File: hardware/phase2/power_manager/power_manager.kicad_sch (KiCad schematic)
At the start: 80 parts, among them J1 1725656, J2 Conn_02x04_Odd_Even, J3 S2B-PH-K-SLFSN, J4 OSTVN04A150, J5 10118194-0001LF, U1 LTC3586EUFE-PBF, U2 TPS60403DBVR, U3 TPS73225DBVR, U4 TPS72325DBVR

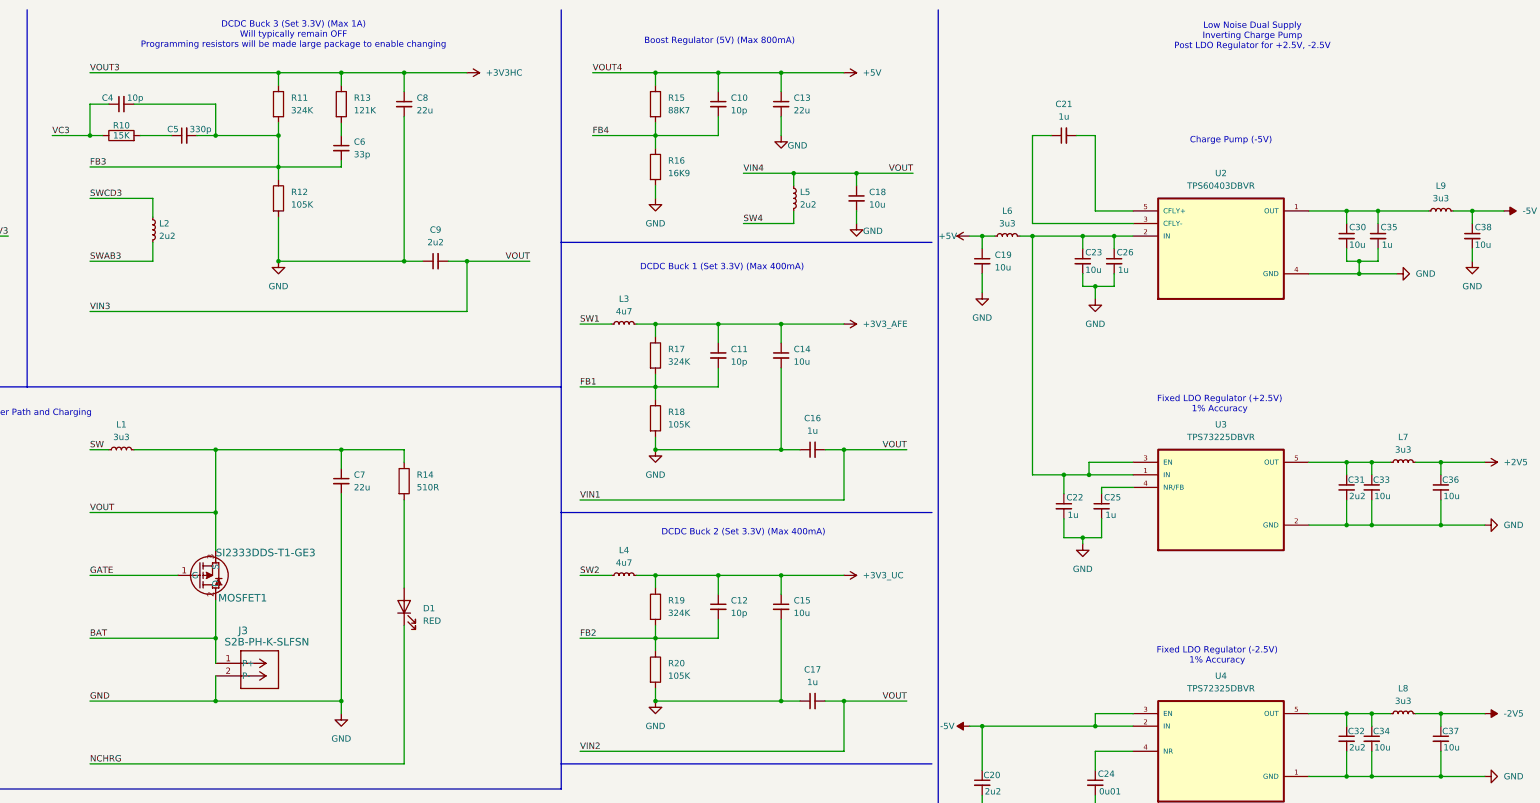
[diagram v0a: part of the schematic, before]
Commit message: Update text on schematic
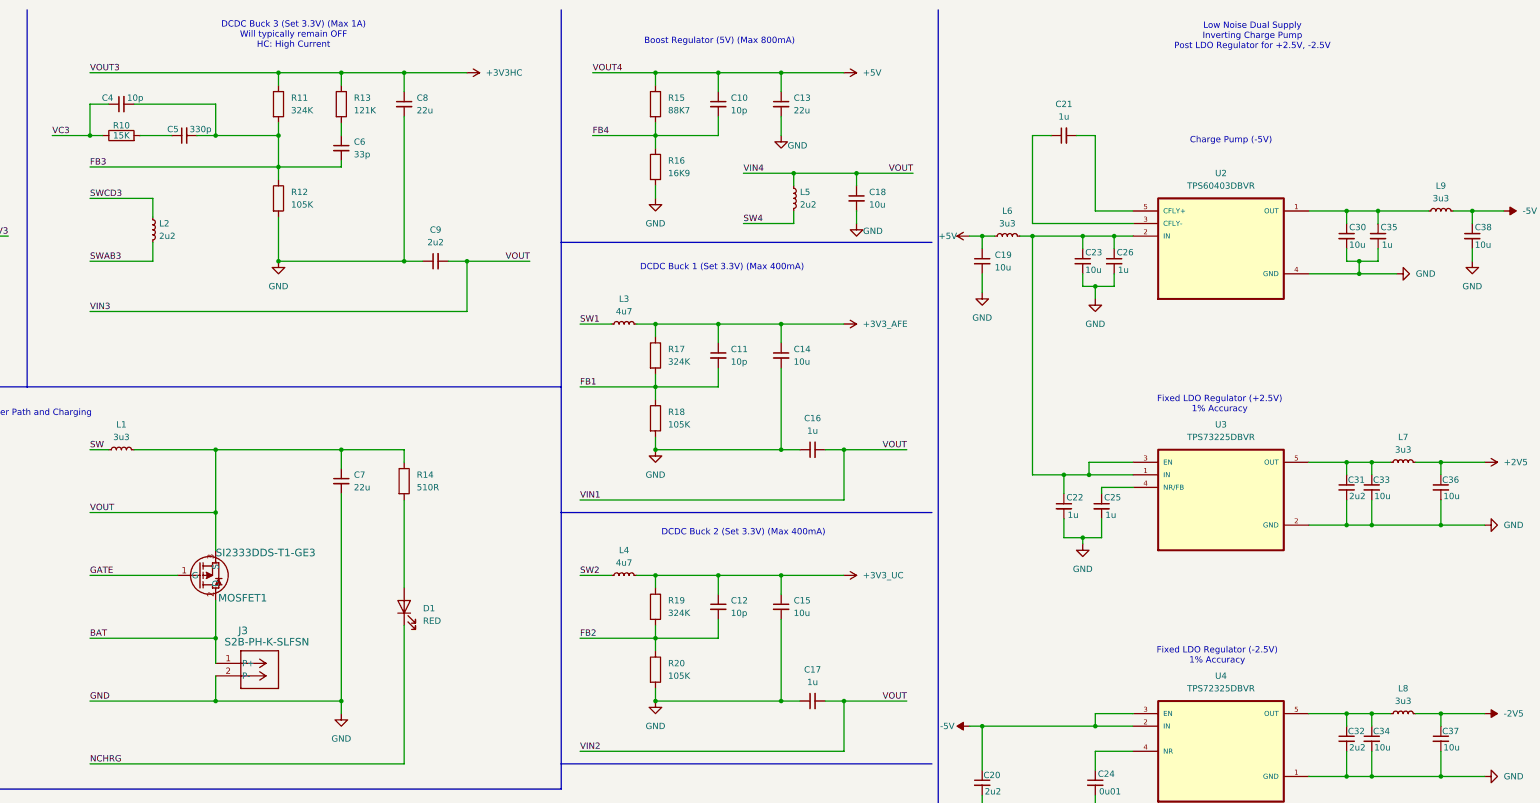
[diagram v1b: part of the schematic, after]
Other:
- note added: "DCDC Buck 3 (Set 3.3V) (Max 1A) Will typically remain OFF HC: High Current"
- note removed: "DCDC Buck 3 (Set 3.3V) (Max 1A) Will typically remain OFF Programming resistors will be made large package to enable changing"
